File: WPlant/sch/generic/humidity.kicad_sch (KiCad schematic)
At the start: 15 parts, among them J11 HSensor, J12 HSensor, J13 HSensor, J14 HSensor, J15 HSensor, J16 HSensor, J17 HSensor, J18 WaterLevel, U12 CD74HCT4051M96, U13 CD74HCT4051M96, U14 SN74LVC1G14DBV

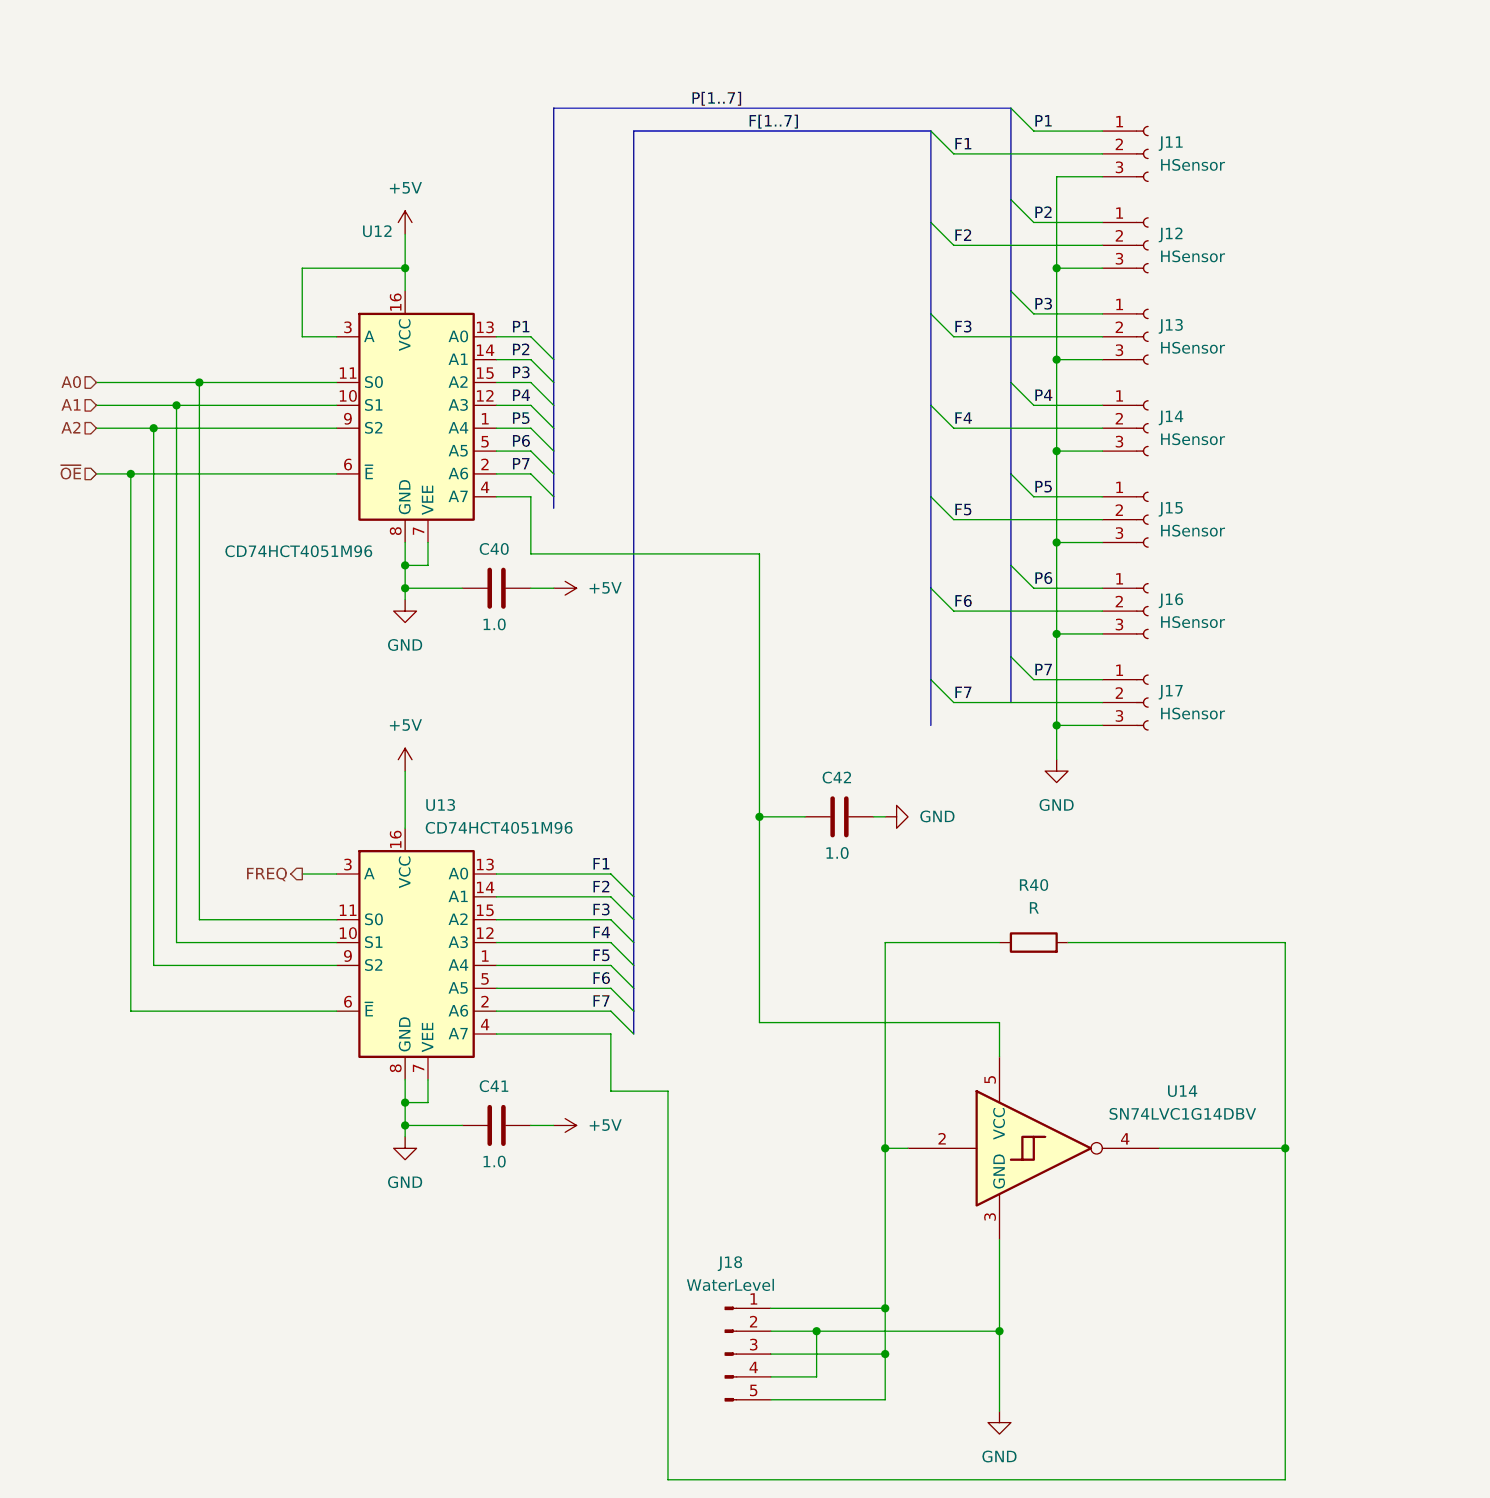
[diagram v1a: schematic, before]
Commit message: Small updates SCH of WP Generic part
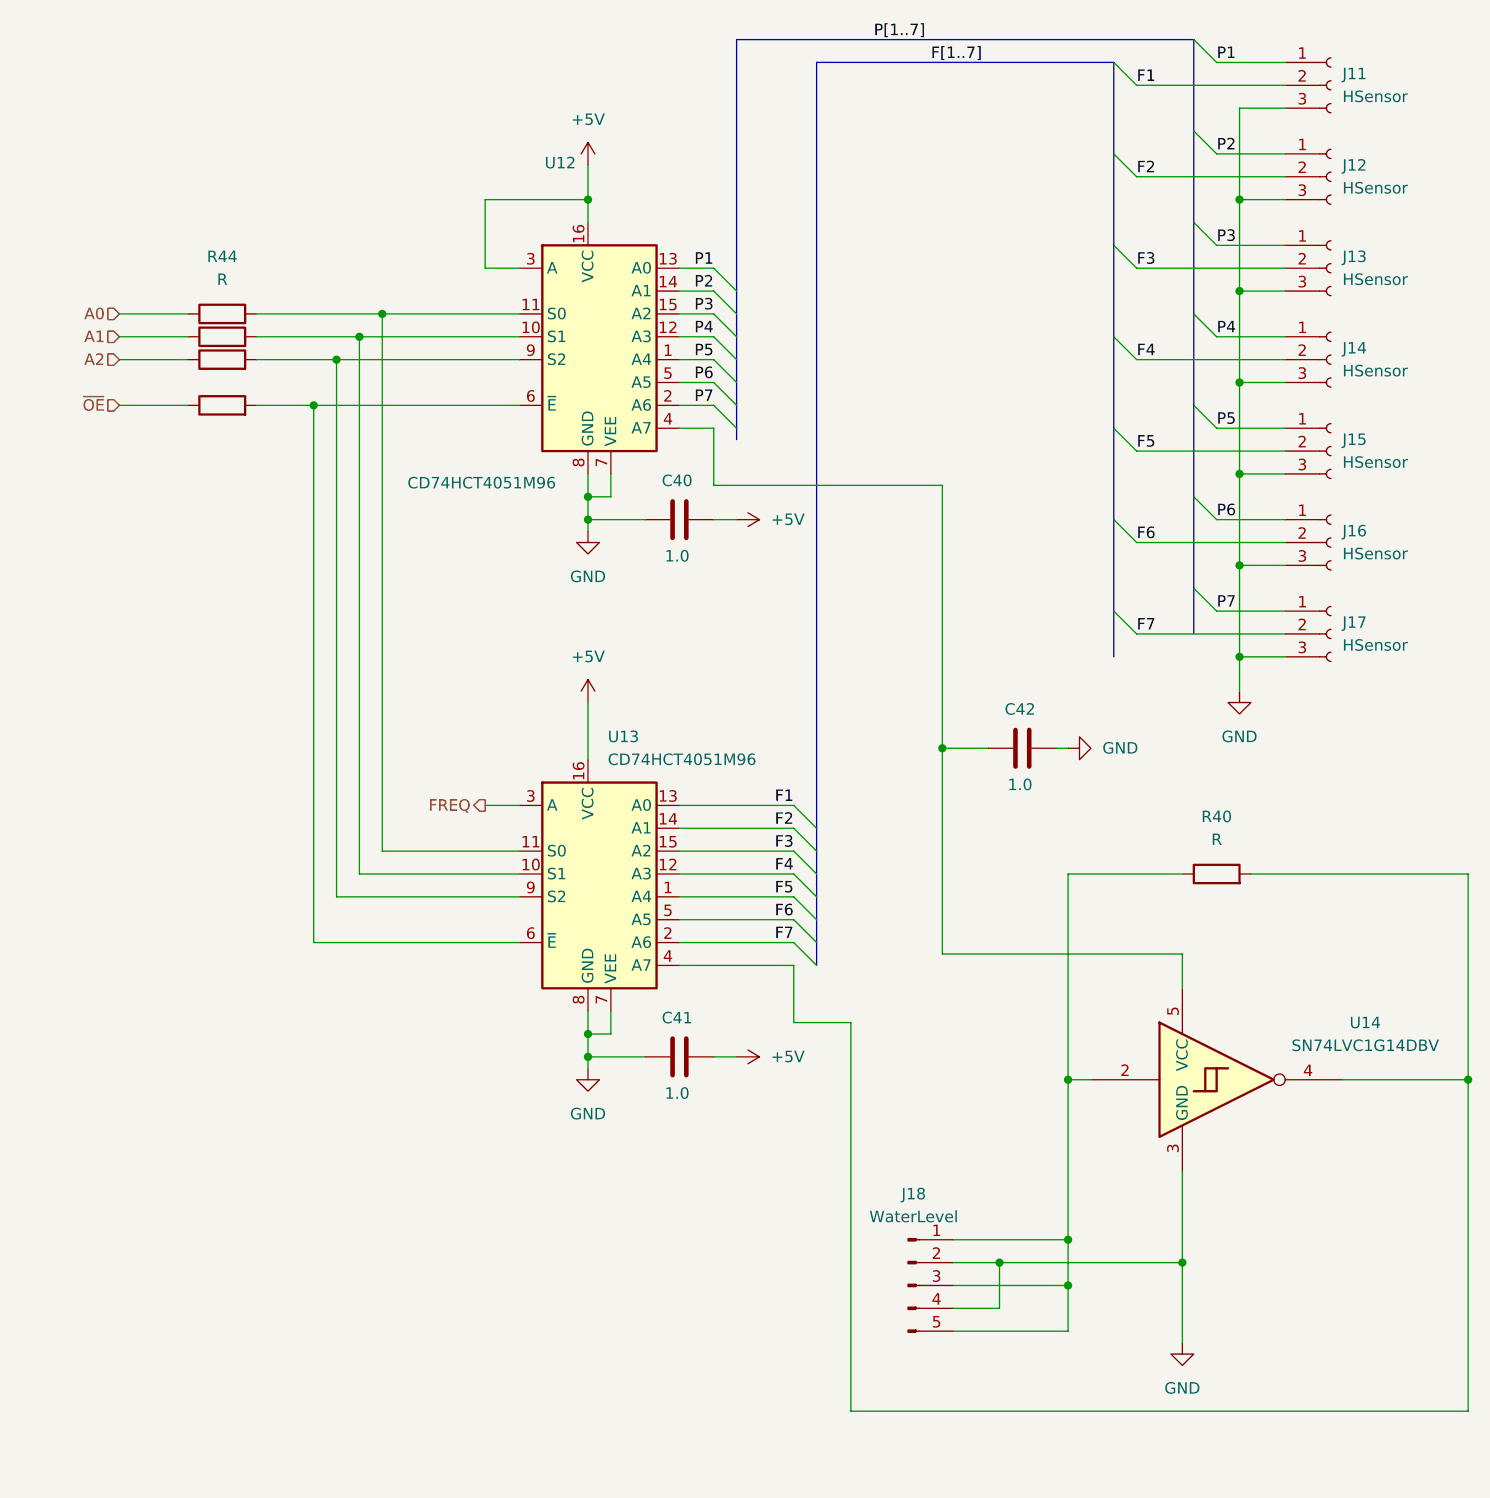
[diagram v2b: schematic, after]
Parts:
- added R44, R45, R46, R47: R, symbol Device:R
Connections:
- net A0: now also R44.1; no longer U12.11 (S0), U13.11 (S0)
- net A1: now also R45.1; no longer U12.10 (S1), U13.10 (S1)
- net A2: now also R46.1; no longer U12.9 (S2), U13.9 (S2)
- net ~{OE}: now also R47.1; no longer U12.6 (~{E}), U13.6 (~{E})
- new net: R45.2, U12.10 (S1), U13.10 (S1)
- new net: R44.2, U12.11 (S0), U13.11 (S0)
- new net: R47.2, U12.6 (~{E}), U13.6 (~{E})
- new net: R46.2, U12.9 (S2), U13.9 (S2)
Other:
- moved on the sheet: C40, C41, C42, J11, J12, J13, J14, J15, J16, J17, J18, R40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

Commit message: Update WP Extension and Generic
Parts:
- added R50: 100, symbol Device:R
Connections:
- net +5V: now also R50.1; no longer U12.3 (A)
- new net: R50.2, U12.3 (A)
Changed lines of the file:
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@@
-	(wire
-		(pts
-			(xy 66.04 46.99) (xy 77.47 46.99)
-		)
-		(stroke
-			(width 0)
-			(type default)
-		)
-	)
 	(wire
 		(pts
@@
 	(wire
 		(pts
-			(xy 69.85 54.61) (xy 66.04 54.61)
+			(xy 69.85 54.61) (xy 67.31 54.61)
 		)
 		(stroke
@@
 	(wire
 		(pts
+			(xy 57.15 54.61) (xy 59.69 54.61)
+		)
+		(stroke
+			(width 0)
+			(type default)
+		)
+	)
+	(wire
+		(pts
 			(xy 175.26 144.78) (xy 161.29 144.78)
 		)
@@
 	(wire
 		(pts
+			(xy 57.15 46.99) (xy 77.47 46.99)
+		)
+		(stroke
+			(width 0)
+			(type default)
+		)
+	)
+	(wire
+		(pts
 			(xy 143.51 154.94) (xy 143.51 165.1)
 		)
@@
 	(wire
 		(pts
+			(xy 57.15 46.99) (xy 57.15 54.61)
+		)
+		(stroke
+			(width 0)
+			(type default)
+		)
+	)
+	(wire
+		(pts
 			(xy 77.47 102.87) (xy 77.47 109.22)
 		)
@@
 		(pts
 			(xy 135.89 72.39) (xy 135.89 82.55)
-		)
-		(stroke
-			(width 0)
-			(type default)
-		)
-	)
-	(wire
-		(pts
-			(xy 66.04 54.61) (xy 66.04 46.99)
 		)
 		(stroke
@@
 					(unit 1)
 				)
+			)
+		)
+	)
+	(symbol
+		(lib_id "Device:R")
+		(at 63.5 54.61 90)
+		(unit 1)
+		(exclude_from_sim no)
+		(in_bom yes)
+		(on_board yes)
+		(dnp no)
+		(fields_autoplaced yes)
+		(property "Reference" "R50"
+			(at 63.5 48.26 90)
+			(effects
+				(font
+					(size 1.27 1.27)
+				)
+			)
+		)
+		(property "Value" "100"
+			(at 63.5 50.8 90)
+			(effects
+				(font
+					(size 1.27 1.27)
+				)
+			)
+		)
+		(property "Footprint" ""
+			(at 63.5 56.388 90)
+			(effects
+				(font
+					(size 1.27 1.27)
+				)
+				(hide yes)
+			)
+		)
+		(property "Datasheet" "~"
+			(at 63.5 54.61 0)
+			(effects
+				(font
+					(size 1.27 1.27)
+				)
+				(hide yes)
+			)
+		)
+		(property "Description" "Resistor"
+			(at 63.5 54.61 0)
+			(effects
+				(font
+					(size 1.27 1.27)
+				)
+				(hide yes)
+			)
+		)
+		(pin "1"
+		)
+		(pin "2"
+		)
+		(instances
+			(project "generic"
+				(path "/71bd3f7f-463d-4a2c-bec7-ca56c2fe6cec/62d9780d-414e-4785-ace8-3a65ab7f9f82"
+					(reference "R50")
+					(unit 1)
+				)

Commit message: Almost finished WP Generic
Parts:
- C40, C41, C42: footprint (none) -> Capacitor_SMD:C_0603_1608Metric_Pad1.08x0.95mm_HandSolder
- J11, J12, J13, J14, J15, J16, J17: footprint (none) -> easyeda2kicad:CONN-TH_DB301R-3.5-3P-GN-S
- J18: footprint (none) -> Connector_JST:JST_XH_B5B-XH-A_1x05_P2.50mm_Vertical
- R40, R44, R45, R46, R47, R50: footprint (none) -> Resistor_SMD:R_0603_1608Metric_Pad0.98x0.95mm_HandSolder
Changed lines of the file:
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@@
 			)
 		)
-		(property "Footprint" ""
+		(property "Footprint" "easyeda2kicad:CONN-TH_DB301R-3.5-3P-GN-S"
 			(at 160.02 44.45 0)
 			(effects
@@
 			)
 		)
-		(property "Footprint" ""
+		(property "Footprint" "easyeda2kicad:CONN-TH_DB301R-3.5-3P-GN-S"
 			(at 160.02 85.09 0)
 			(effects
@@
 			)
 		)
-		(property "Footprint" ""
+		(property "Footprint" "Capacitor_SMD:C_0603_1608Metric_Pad1.08x0.95mm_HandSolder"
 			(at 129.54 106.9848 0)
 			(effects
@@
 			)
 		)
-		(property "Footprint" ""
+		(property "Footprint" "Connector_JST:JST_XH_B5B-XH-A_1x05_P2.50mm_Vertical"
 			(at 113.03 167.64 0)
 			(effects
@@
 			)
 		)
-		(property "Footprint" ""
+		(property "Footprint" "easyeda2kicad:CONN-TH_DB301R-3.5-3P-GN-S"
 			(at 160.02 95.25 0)
 			(effects
@@
 			)
 		)
-		(property "Footprint" ""
+		(property "Footprint" "Resistor_SMD:R_0603_1608Metric_Pad0.98x0.95mm_HandSolder"
 			(at 63.5 56.388 90)
 			(effects
@@
 			)
 		)
-		(property "Footprint" ""
+		(property "Footprint" "Resistor_SMD:R_0603_1608Metric_Pad0.98x0.95mm_HandSolder"
 			(at 36.83 66.548 90)
 			(effects
@@
 			)
 		)
-		(property "Footprint" ""
+		(property "Footprint" "Capacitor_SMD:C_0603_1608Metric_Pad1.08x0.95mm_HandSolder"
 			(at 91.44 141.2748 0)
 			(effects
@@
 			)
 		)
-		(property "Footprint" ""
+		(property "Footprint" "Resistor_SMD:R_0603_1608Metric_Pad0.98x0.95mm_HandSolder"
 			(at 147.32 123.698 90)
 			(effects
@@
 			)
 		)
-		(property "Footprint" ""
+		(property "Footprint" "Resistor_SMD:R_0603_1608Metric_Pad0.98x0.95mm_HandSolder"
 			(at 36.83 64.008 90)
 			(effects
@@
 			)
 		)
-		(property "Footprint" ""
+		(property "Footprint" "easyeda2kicad:CONN-TH_DB301R-3.5-3P-GN-S"
 			(at 160.02 74.93 0)
 			(effects
@@
 			)
 		)
-		(property "Footprint" ""
+		(property "Footprint" "easyeda2kicad:CONN-TH_DB301R-3.5-3P-GN-S"
 			(at 160.02 34.29 0)
 			(effects
@@
 			)
 		)
-		(property "Footprint" ""
+		(property "Footprint" "easyeda2kicad:CONN-TH_DB301R-3.5-3P-GN-S"
 			(at 160.02 54.61 0)
 			(effects
@@
 			)
 		)
-		(property "Footprint" ""
+		(property "Footprint" "easyeda2kicad:CONN-TH_DB301R-3.5-3P-GN-S"
 			(at 160.02 64.77 0)
 			(effects
@@
 			)
 		)
-		(property "Footprint" ""
+		(property "Footprint" "Resistor_SMD:R_0603_1608Metric_Pad0.98x0.95mm_HandSolder"
 			(at 36.83 71.628 90)
 			(effects
@@
 			)
 		)
-		(property "Footprint" ""
+		(property "Footprint" "Capacitor_SMD:C_0603_1608Metric_Pad1.08x0.95mm_HandSolder"
 			(at 91.44 81.5848 0)
 			(effects
@@
 			)
 		)
-		(property "Footprint" ""
+		(property "Footprint" "Resistor_SMD:R_0603_1608Metric_Pad0.98x0.95mm_HandSolder"
 			(at 36.83 61.468 90)
 			(effects

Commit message: Update WP Generic packages assignment
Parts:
- U14: footprint Package_TO_SOT_SMD:SOT-23-5 -> Package_TO_SOT_SMD:SOT-23-5_HandSoldering
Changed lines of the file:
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@@
 			)
 		)
-		(property "Footprint" "Package_TO_SOT_SMD:SOT-23-5"
+		(property "Footprint" "Package_TO_SOT_SMD:SOT-23-5_HandSoldering"
 			(at 148.59 151.13 0)
 			(effects
